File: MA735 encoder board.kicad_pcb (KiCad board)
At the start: 2 copper layers, 5.7 x 105.4 mm, 4 parts, among them J1 FPC contacts 0.3mm, U1 MA735GGU-Z

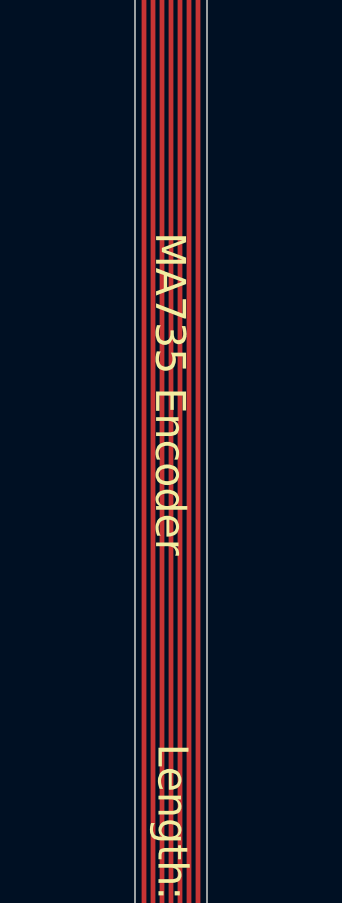
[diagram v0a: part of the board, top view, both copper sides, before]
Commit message: Updated graphics
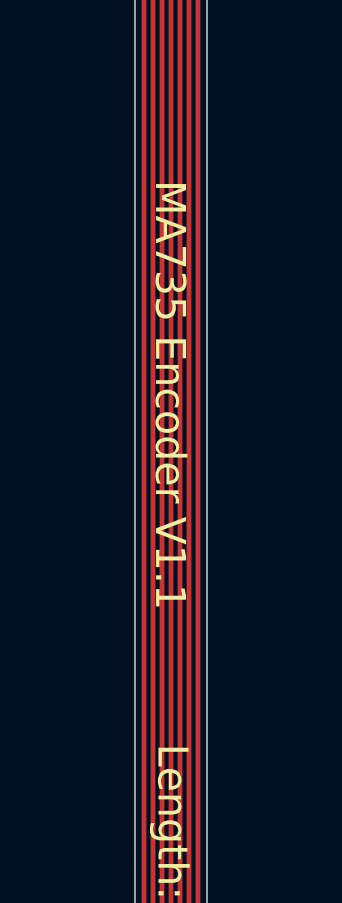
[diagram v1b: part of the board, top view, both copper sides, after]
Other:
- board text added: "MA735 Encoder ${REVISION}"
- board text removed: "MA735 Encoder"
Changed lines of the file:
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@@
 		)
 	)
-	(gr_text "MA735 Encoder"
-		(at 152.18 90.31 270)
+	(gr_text "MA735 Encoder ${REVISION}"
+		(at 152.18 88.57 270)
 		(layer "F.SilkS")
 		(effects
@@
 			)
 			(justify left top)
+		)
+		(border yes)
+		(stroke
+			(width 0.1)
+			(type solid)
+		)
+	)
+	(gr_text_box "0.1mm thick stiffener"
+		(start 168.54 59.94)
+		(end 181.76 65.37)
+		(margins 1.0025 1.0025 1.0025 1.0025)
+		(layer "User.2")
+		(effects
+			(font
+				(size 1 1)
+				(thickness 0.15)
+			)
+			(justify left top)

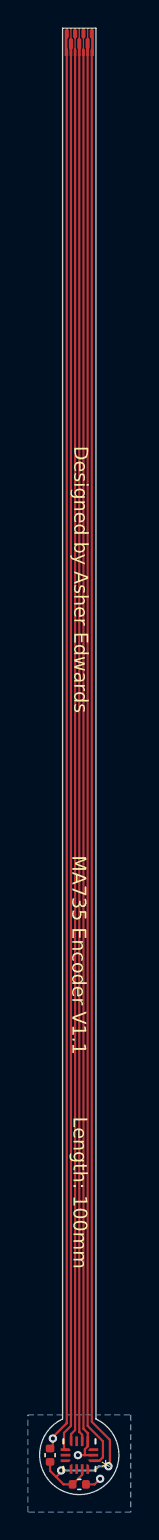
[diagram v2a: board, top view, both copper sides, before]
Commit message: Rounded Tracks
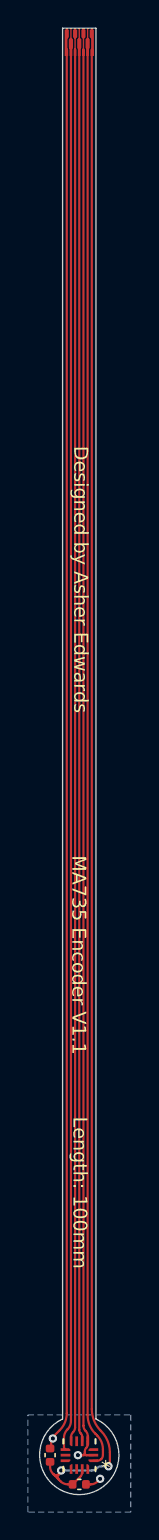
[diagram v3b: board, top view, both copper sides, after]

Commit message: Fixed errors in DRC
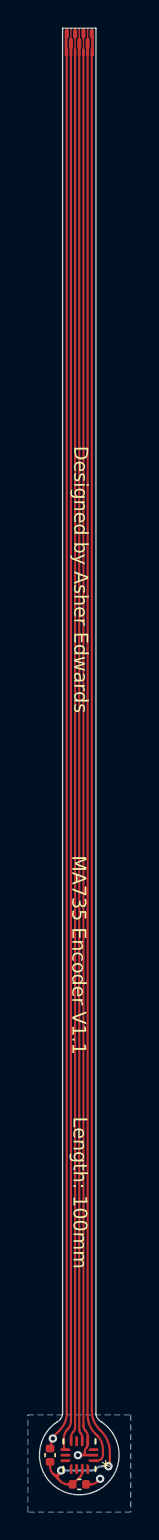
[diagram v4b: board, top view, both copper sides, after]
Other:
- board size 5.7 x 105.4 mm -> 5.7 x 105.5 mm
